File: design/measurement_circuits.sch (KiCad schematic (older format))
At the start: 0 parts

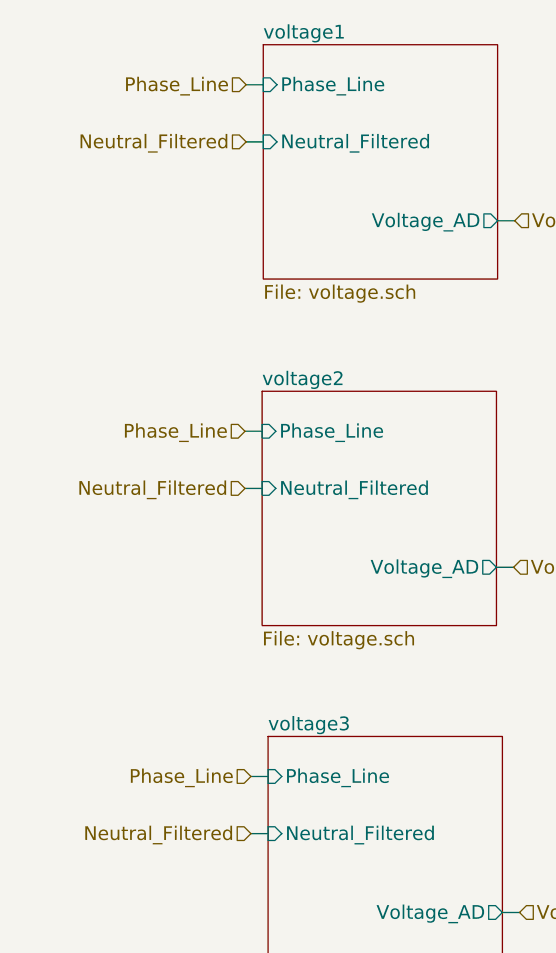
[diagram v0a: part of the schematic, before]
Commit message: Fix connection problems.
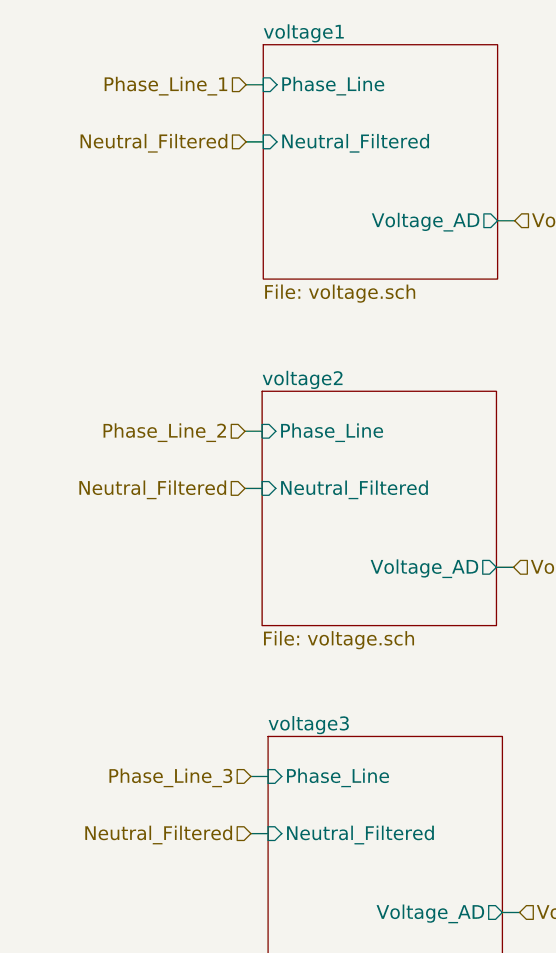
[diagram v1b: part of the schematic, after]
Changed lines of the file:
@@
 $EndSheet
 Text HLabel 1690 1078 0    60   Input ~ 0
-Phase_Line
+Phase_Line_1
 Text HLabel 4842 1071 0    60   Input ~ 0
 CT1_1
@@
 $EndSheet
 Text HLabel 1685 2594 0    60   Input ~ 0
-Phase_Line
+Phase_Line_2
 Text HLabel 2860 3189 2    60   Input ~ 0
 Voltage_AD_2
@@
 $EndSheet
 Text HLabel 1711 4104 0    60   Input ~ 0
-Phase_Line
+Phase_Line_3
 Text HLabel 2886 4699 2    60   Input ~ 0
 Voltage_AD_3
